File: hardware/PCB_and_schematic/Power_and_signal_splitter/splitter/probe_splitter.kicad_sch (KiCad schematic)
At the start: 14 parts, among them J2 SIGNAL_TERMINAL, J3 DC_POWER_SUPPLY, J4 DC_POWER_SUPPLY, J5 DC_POWER_SUPPLY, J6 DIODE_PROBE, J7 OPTICAL_PROBE, J8 UNUSED, U1 L7812

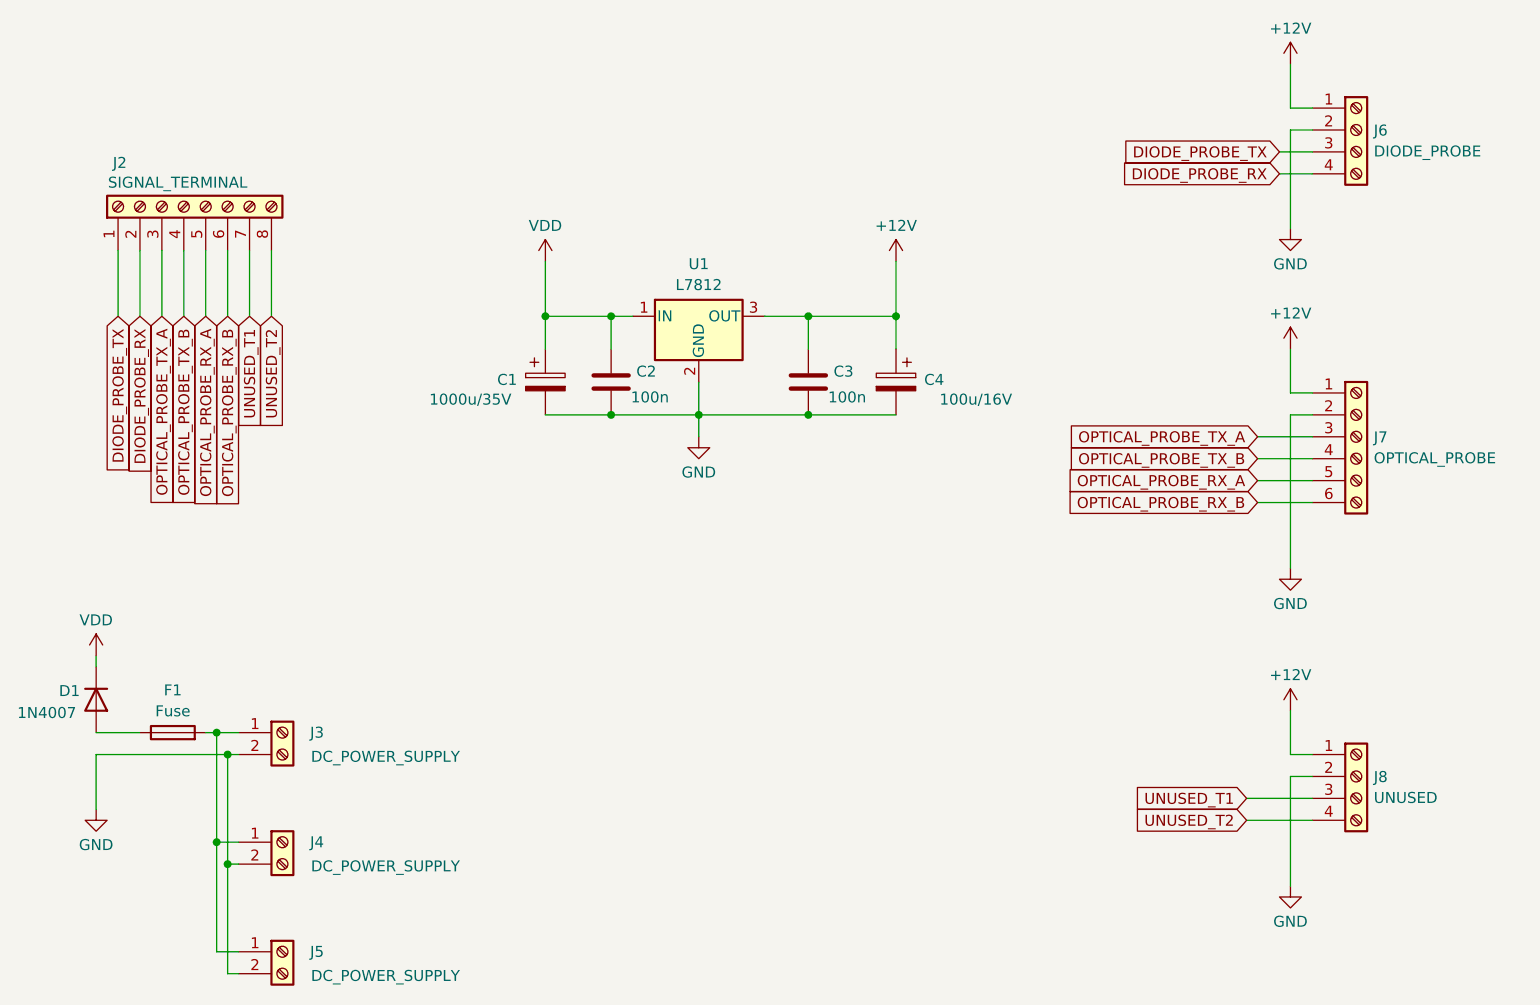
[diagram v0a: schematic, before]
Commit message: Splitter and connector footprints, progress with balancer pcb routing
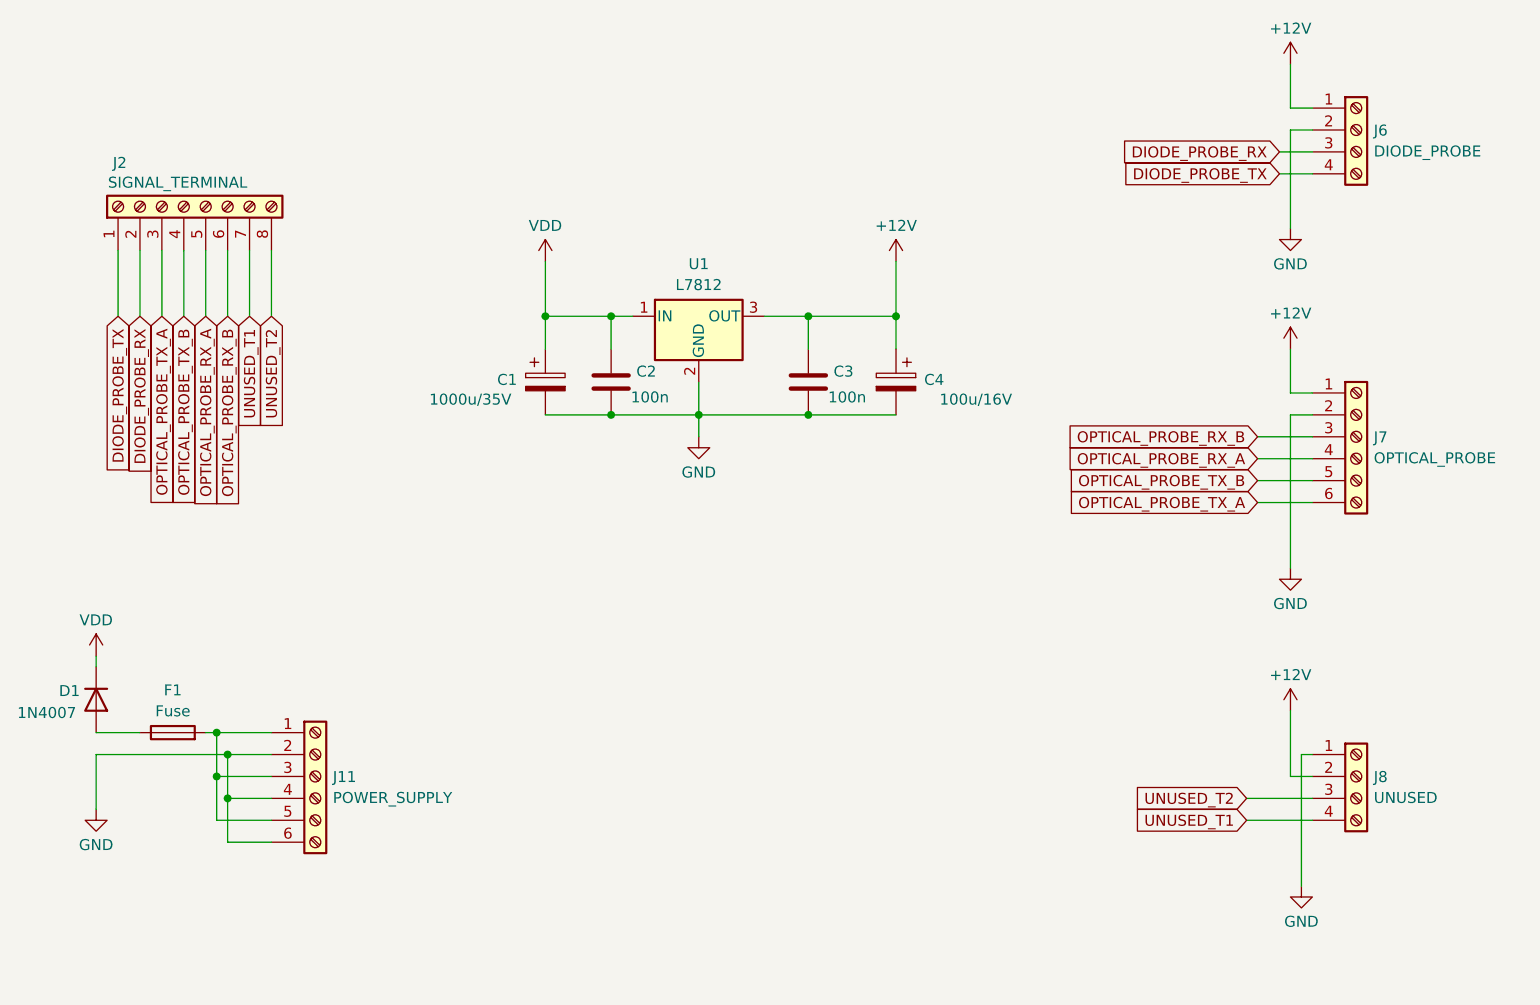
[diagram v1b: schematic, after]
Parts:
- removed J3, J4, J5: DC_POWER_SUPPLY, TerminalBlock:TerminalBlock_Altech_AK300-2_P5.00mm, symbol Connector:Screw_Terminal_01x02
- added J11: POWER_SUPPLY, My-Footprints-connectors:Screw-Terminal-P6-rast-5mm-6,7x30, symbol Connector:Screw_Terminal_01x06
- C1: footprint Capacitor_THT:CP_Radial_D10.0mm_P3.80mm -> Capacitor_THT:CP_Radial_D8.0mm_P3.50mm
- C2, C3: footprint Capacitor_SMD:C_0805_2012Metric -> Capacitor_THT:C_Disc_D4.7mm_W2.5mm_P5.00mm
- J2: footprint TerminalBlock:TerminalBlock_bornier-8_P5.08mm -> My-Footprints-connectors:WAGO-255-8P
- J6, J8: footprint TerminalBlock:TerminalBlock_Altech_AK300-4_P5.00mm -> My-Footprints-connectors:WAGO-739-4P
- J7: footprint TerminalBlock:TerminalBlock_bornier-6_P5.08mm -> My-Footprints-connectors:HDQ-250-6P
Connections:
- net +12V: now also J8.2 (Pin_2); no longer J8.1 (Pin_1)
- net DIODE_PROBE_RX: now also J6.3 (Pin_3); no longer J6.4 (Pin_4)
- net DIODE_PROBE_TX: now also J6.4 (Pin_4); no longer J6.3 (Pin_3)
- net GND: now also J8.1 (Pin_1), J11.2 (Pin_2), J11.4 (Pin_4), J11.6 (Pin_6); no longer J8.2 (Pin_2)
- net OPTICAL_PROBE_RX_A: now also J7.4 (Pin_4); no longer J7.5 (Pin_5)
- net OPTICAL_PROBE_RX_B: now also J7.3 (Pin_3); no longer J7.6 (Pin_6)
- net OPTICAL_PROBE_TX_A: now also J7.6 (Pin_6); no longer J7.3 (Pin_3)
- net OPTICAL_PROBE_TX_B: now also J7.5 (Pin_5); no longer J7.4 (Pin_4)
- net UNUSED_T1: now also J8.4 (Pin_4); no longer J8.3 (Pin_3)
- net UNUSED_T2: now also J8.3 (Pin_3); no longer J8.4 (Pin_4)
- net at F1.2: now also J11.1 (Pin_1), J11.3 (Pin_3), J11.5 (Pin_5)

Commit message: splitter components adjustment
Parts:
- C1: footprint Capacitor_THT:CP_Radial_D8.0mm_P3.50mm -> Capacitor_THT:CP_Radial_D10.0mm_P5.00mm
- C4: footprint Capacitor_THT:CP_Radial_D8.0mm_P3.50mm -> Capacitor_THT:CP_Radial_D6.3mm_P2.50mm
- F1: footprint Fuse:Fuseholder_Clip-5x20mm_Eaton_1A5601-01_Inline_P20.80x6.76mm_D1.70mm_Horizontal -> My-Footprints:Fuseholder_Clip-5x20mm_Eaton_1A5601-01_Inline_P20.80x6.76mm_D1.70mm_Horizontal
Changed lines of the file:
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@@
 			)
 		)
-		(property "Footprint" "Capacitor_THT:CP_Radial_D8.0mm_P3.50mm"
+		(property "Footprint" "Capacitor_THT:CP_Radial_D6.3mm_P2.50mm"
 			(at 150.1648 67.31 0)
 			(effects
@@
 			)
 		)
-		(property "Footprint" "Capacitor_THT:CP_Radial_D8.0mm_P3.50mm"
+		(property "Footprint" "Capacitor_THT:CP_Radial_D10.0mm_P5.00mm"
 			(at 111.4552 67.31 0)
 			(effects
@@
 			)
 		)
-		(property "Footprint" "Fuse:Fuseholder_Clip-5x20mm_Eaton_1A5601-01_Inline_P20.80x6.76mm_D1.70mm_Horizontal"
+		(property "Footprint" "My-Footprints:Fuseholder_Clip-5x20mm_Eaton_1A5601-01_Inline_P20.80x6.76mm_D1.70mm_Horizontal"
 			(at 67.31 105.918 90)
 			(effects
